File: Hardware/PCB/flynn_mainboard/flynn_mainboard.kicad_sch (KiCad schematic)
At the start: 0 parts

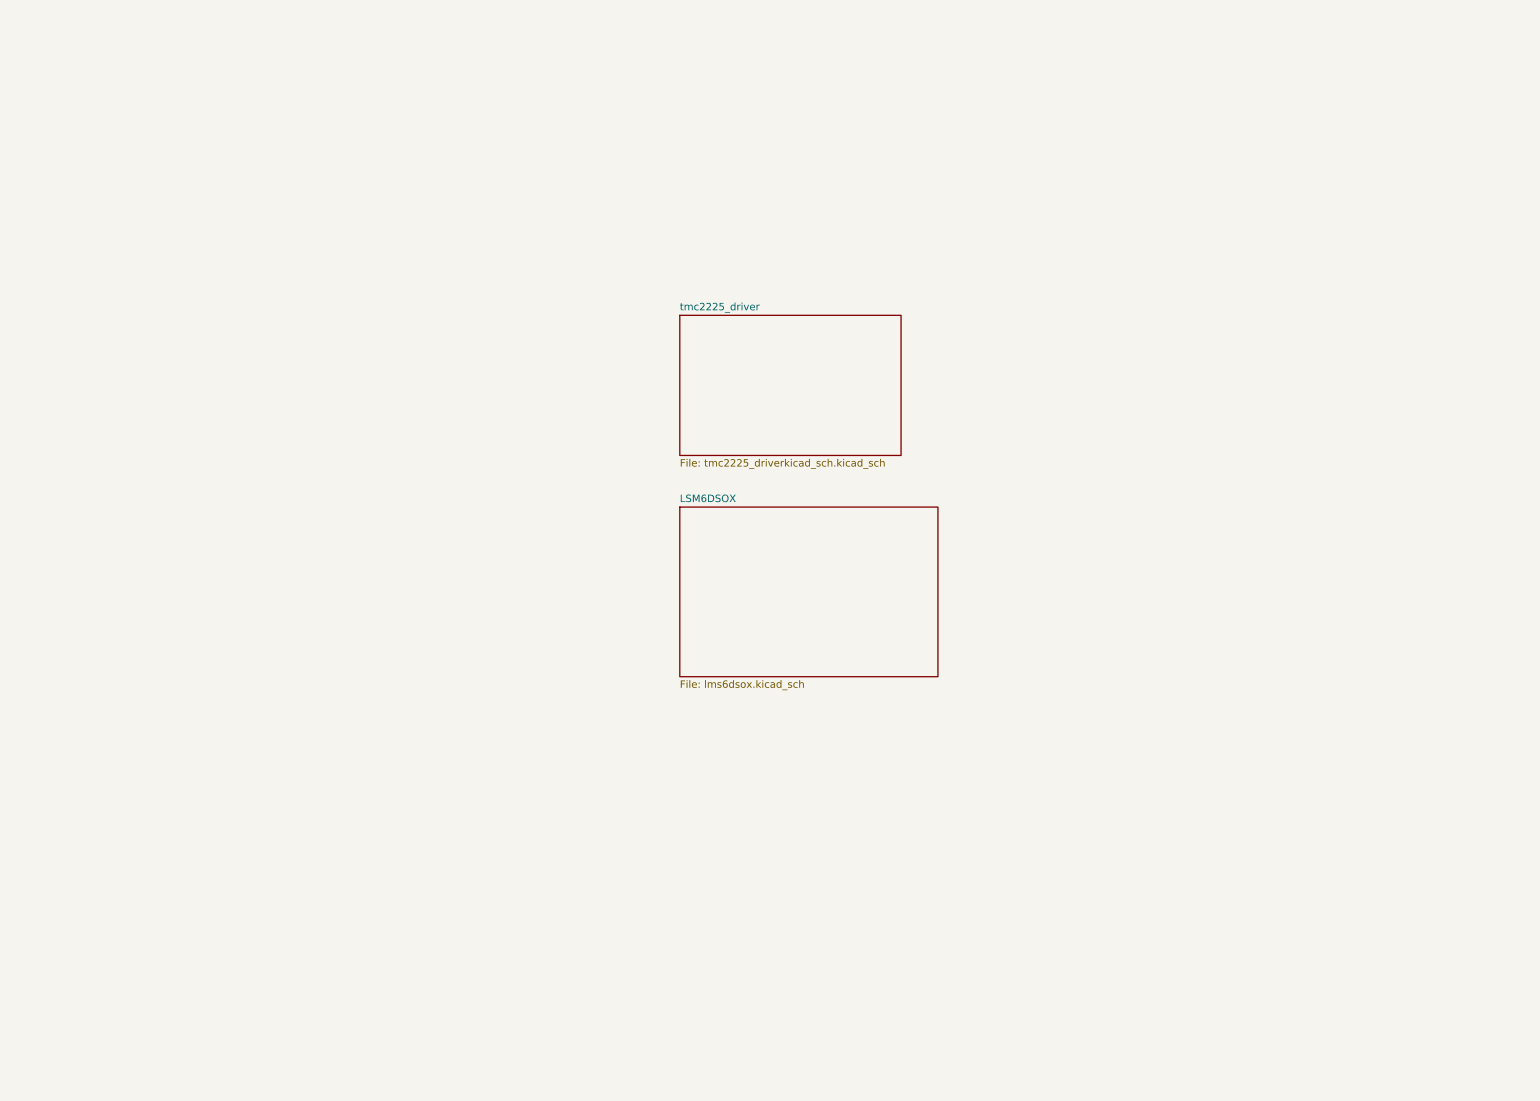
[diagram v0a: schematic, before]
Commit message: Ajout du schéma
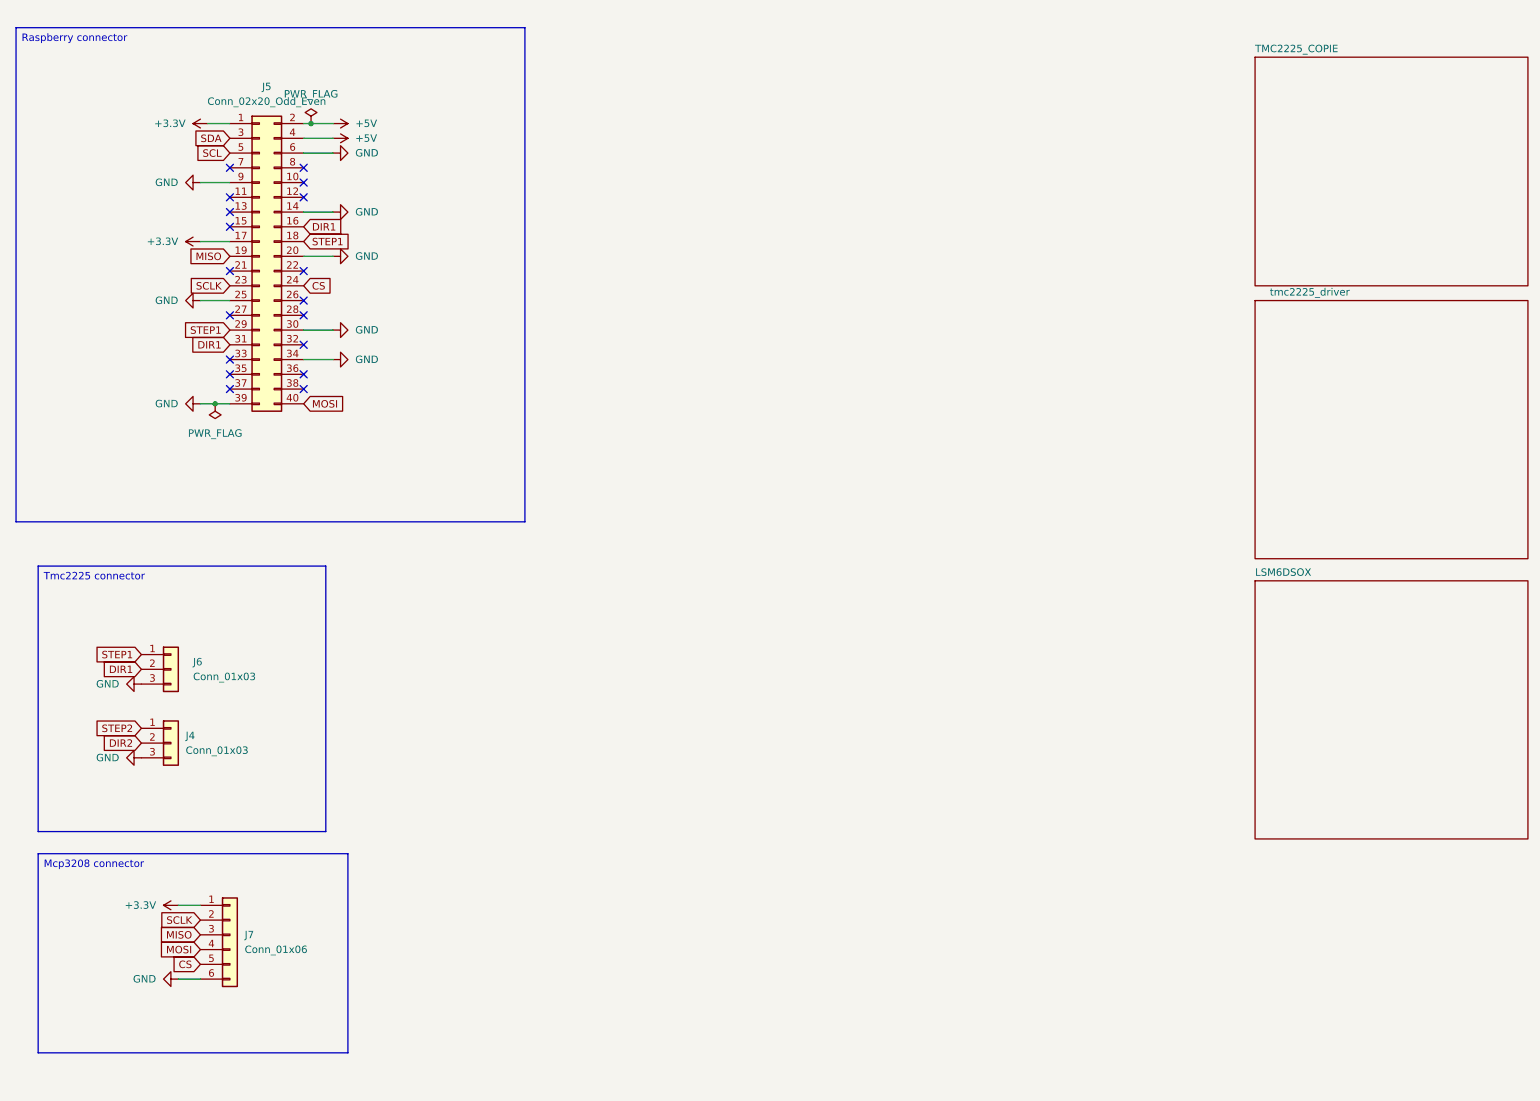
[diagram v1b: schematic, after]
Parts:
- added J4, J6: Conn_01x03, symbol Connector_Generic:Conn_01x03
- added J5: Conn_02x20_Odd_Even, symbol Connector_Generic:Conn_02x20_Odd_Even
- added J7: Conn_01x06, symbol Connector_Generic:Conn_01x06
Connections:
- new net +3.3V: J5.1 (Pin_1), J5.17 (Pin_17), J7.1 (Pin_1)
- new net +5V: J5.2 (Pin_2), J5.4 (Pin_4)
- new net CS: J5.24 (Pin_24), J7.5 (Pin_5)
- new net DIR1: J5.16 (Pin_16), J5.31 (Pin_31), J6.2 (Pin_2)
- new net DIR2: J4.2 (Pin_2)
- new net GND: J4.3 (Pin_3), J5.14 (Pin_14), J5.20 (Pin_20), J5.25 (Pin_25), J5.30 (Pin_30), J5.34 (Pin_34), J5.39 (Pin_39), J5.6 (Pin_6), J5.9 (Pin_9), J6.3 (Pin_3), J7.6 (Pin_6)
- new net MISO: J5.19 (Pin_19), J7.3 (Pin_3)
- new net MOSI: J5.40 (Pin_40), J7.4 (Pin_4)
- new net SCL: J5.5 (Pin_5)
- new net SCLK: J5.23 (Pin_23), J7.2 (Pin_2)
- new net SDA: J5.3 (Pin_3)
- new net STEP1: J5.18 (Pin_18), J5.29 (Pin_29), J6.1 (Pin_1)
- new net STEP2: J4.1 (Pin_1)
- no-connect marks 0 -> 18
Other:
- added sheet TMC2225_COPIE (untitled.kicad_sch)

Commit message: Journaling Update
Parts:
- removed J4, J6: Conn_01x03, symbol Connector_Generic:Conn_01x03
- added C17: 330u, Capacitor_SMD:CP_Elec_6.3x5.4, symbol Device:C_Polarized
- added C18, C8: 100n, Capacitor_SMD:C_0603_1608Metric, symbol Device:C_Small
- added D4, D5: LED, LED_SMD:LED_0603_1608Metric, symbol Device:LED
- added H1, H3, H5, H7: MountingHole_Pad, MountingHole:MountingHole_2.7mm_M2.5_Pad, symbol Mechanical:MountingHole_Pad
- added J2: Conn_01x02, Connector_JST:JST_EH_B2B-EH-A_1x02_P2.50mm_Vertical, symbol Connector_Generic:Conn_01x02
- added R6, R8: 6.8k, Resistor_SMD:R_0603_1608Metric, symbol Device:R
- J5: value Conn_02x20_Odd_Even -> Rpi 2W Zéro; footprint (none) -> Connector_PinSocket_2.54mm:PinSocket_2x20_P2.54mm_Vertical
- J7: footprint (none) -> Connector_JST:JST_PH_B6B-PH-K_1x06_P2.00mm_Vertical
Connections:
- net +3.3V: now also J7.6 (Pin_6), C8.2, R8.1; no longer J7.1 (Pin_1)
- net DIR1: now also J5.22 (Pin_22), J5.32 (Pin_32); no longer J5.16 (Pin_16), J5.31 (Pin_31)
- net DIR2: now also J5.31 (Pin_31)
- net GND: now also J7.1 (Pin_1), C17.2, C18.2, C8.1, D4.1 (K), D5.1 (K), H1.1, H3.1, H5.1, H7.1, J2.1 (Pin_1); no longer J7.6 (Pin_6)
- net MISO: now also J5.21 (Pin_21); no longer J5.19 (Pin_19)
- net MOSI: now also J5.19 (Pin_19); no longer J5.40 (Pin_40)
- net STEP2: now also J5.33 (Pin_33)
- net STEP1: no longer names the net of J5.18 (Pin_18)
- net STEP1: no longer J5.29 (Pin_29)
- new net: D5.2 (A), R8.2
- new net: D4.2 (A), R6.2
- new net VCC: C17.1, C18.1, J2.2 (Pin_2), R6.1
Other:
- removed sheet TMC2225_COPIE
- added sheet tmc2225_driver1 (tmc2225_driverkicad_sch.kicad_sch)
- sheet tmc2225_driver ports: added DIR, STEP; removed none
- note added: "BATTERY"
- note added: "FIXING HOLES"
- note added: "LED"
- note added: "MCP3208 CONNECTOR"
- moved on the sheet: J5, J7
